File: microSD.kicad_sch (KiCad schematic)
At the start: 10 parts, among them IC1 4050D, IC2 LP298XS, X1 MICROSD

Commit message: added drawing sheet
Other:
- title: (none) -> microSD
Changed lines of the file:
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@@
 	(generator_version "8.0")
 	(paper "A4")
+	(title_block
+		(title "microSD")
+		(date "2024-03-06")
+	)
 	(junction
 		(at 119.38 109.22)

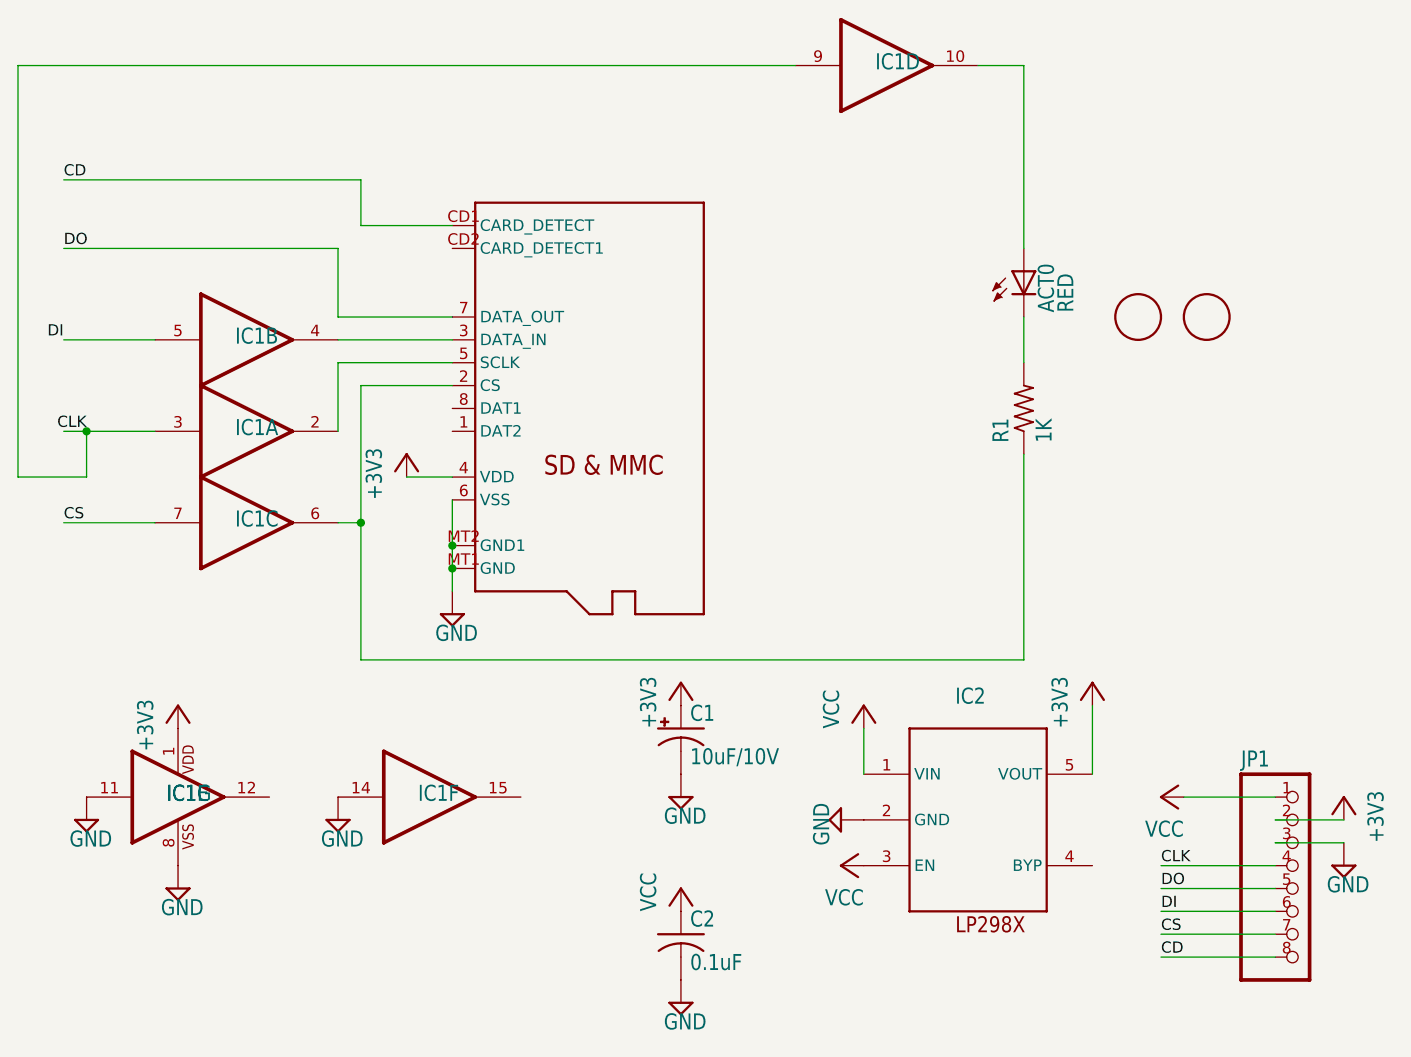
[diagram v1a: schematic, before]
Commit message: fully migrated to KiCad
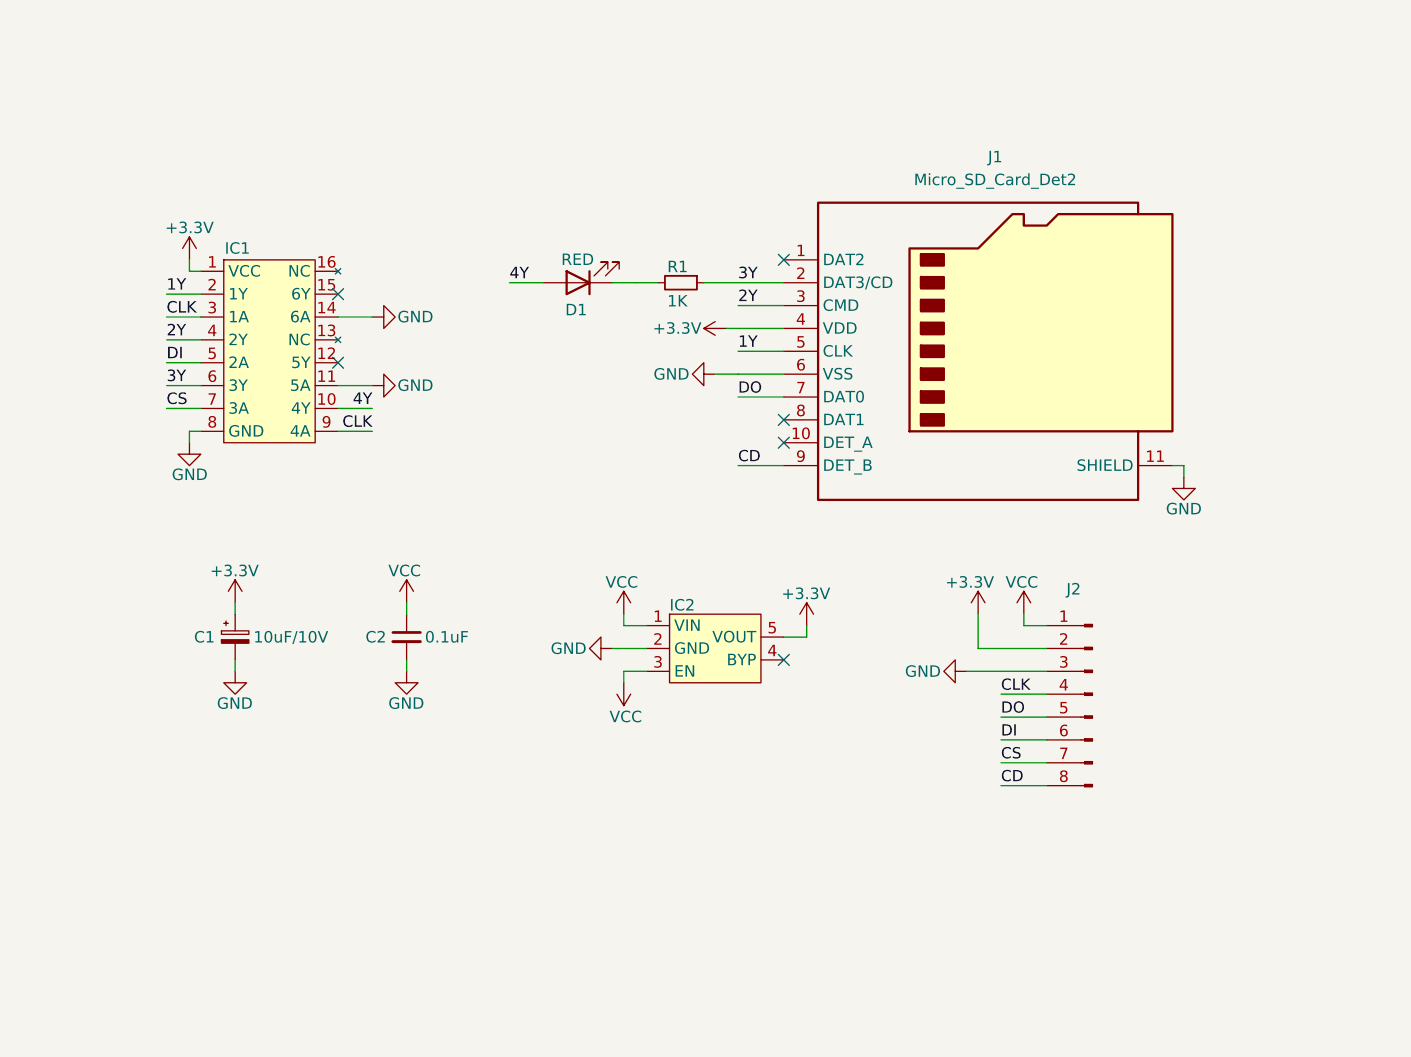
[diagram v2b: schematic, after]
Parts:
- removed ACT0: RED, microSD:CHIP-LED0805, symbol microSD-eagle-import:LEDCHIP-LED0805
- removed IC1: 4050D, microSD:SO16, symbol microSD-eagle-import:4050D
- removed R1: 1K, microSD:R0805, symbol microSD-eagle-import:R-US_R0805
- removed U$1, U$2: FIDUCIAL, microSD:FIDUCIAL_1MM, symbol microSD-eagle-import:FIDUCIAL
- removed X1: MICROSD, microSD:MICROSD, symbol microSD-eagle-import:MICROSD
- added D1: RED, LED_SMD:LED_0805_2012Metric, symbol Device:LED
- added IC1: ~, Package_SO:SOIC-16_3.9x9.9mm_P1.27mm, symbol external_library:74HC4050D
- added J1: Micro_SD_Card_Det2, external_footprints:GCT_MEM2061-01-188-00-A_REVA, symbol Connector:Micro_SD_Card_Det2
- added R1: 1K, Resistor_SMD:R_0805_2012Metric, symbol Device:R_Small
- C1: footprint microSD:A_3216-18R -> Capacitor_Tantalum_SMD:CP_EIA-3216-18_Kemet-A; symbol microSD-eagle-import:CPOL-USA/3216-18R -> Device:C_Polarized_Small
- C2: footprint microSD:C0805K -> Capacitor_SMD:C_0805_2012Metric; symbol microSD-eagle-import:C-USC0805K -> Device:C_Small
- IC2: footprint microSD:SOT23-5L -> Package_TO_SOT_SMD:SOT-23-5; symbol microSD-eagle-import:LP298XS -> external_library:LP2985A
- J2: renamed from JP1; footprint microSD:1X08-BIG -> Connector_PinHeader_2.54mm:PinHeader_1x08_P2.54mm_Vertical; symbol microSD-eagle-import:PINHD-1X8BIG -> Connector:Conn_01x08_Pin
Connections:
- net CD: now also J1.9 (DET_B)
- net CLK: now also IC1.3 (1A), IC1.9 (4A)
- net CS: now also IC1.7 (3A)
- net DI: now also IC1.5 (2A)
- net DO: now also J1.7 (DAT0)
- net GND: now also C1.2, IC1.11 (5A), IC1.14 (6A), IC1.8 (GND), J1.11 (SHIELD), J1.6 (VSS); no longer C1.-
- net +3V3 renamed +3.3V
- net +3.3V: now also C1.1, IC1.1 (VCC), J1.4 (VDD); no longer C1.+
- new net: D1.1 (K), R1.2
- new net 1Y: IC1.2 (1Y), J1.5 (CLK)
- new net 2Y: IC1.4 (2Y), J1.3 (CMD)
- new net 3Y: IC1.6 (3Y), J1.2 (DAT3/CD), R1.1
- new net 4Y: D1.2 (A), IC1.10 (4Y)
- no-connect marks 0 -> 6

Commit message: added info to generate BOM file
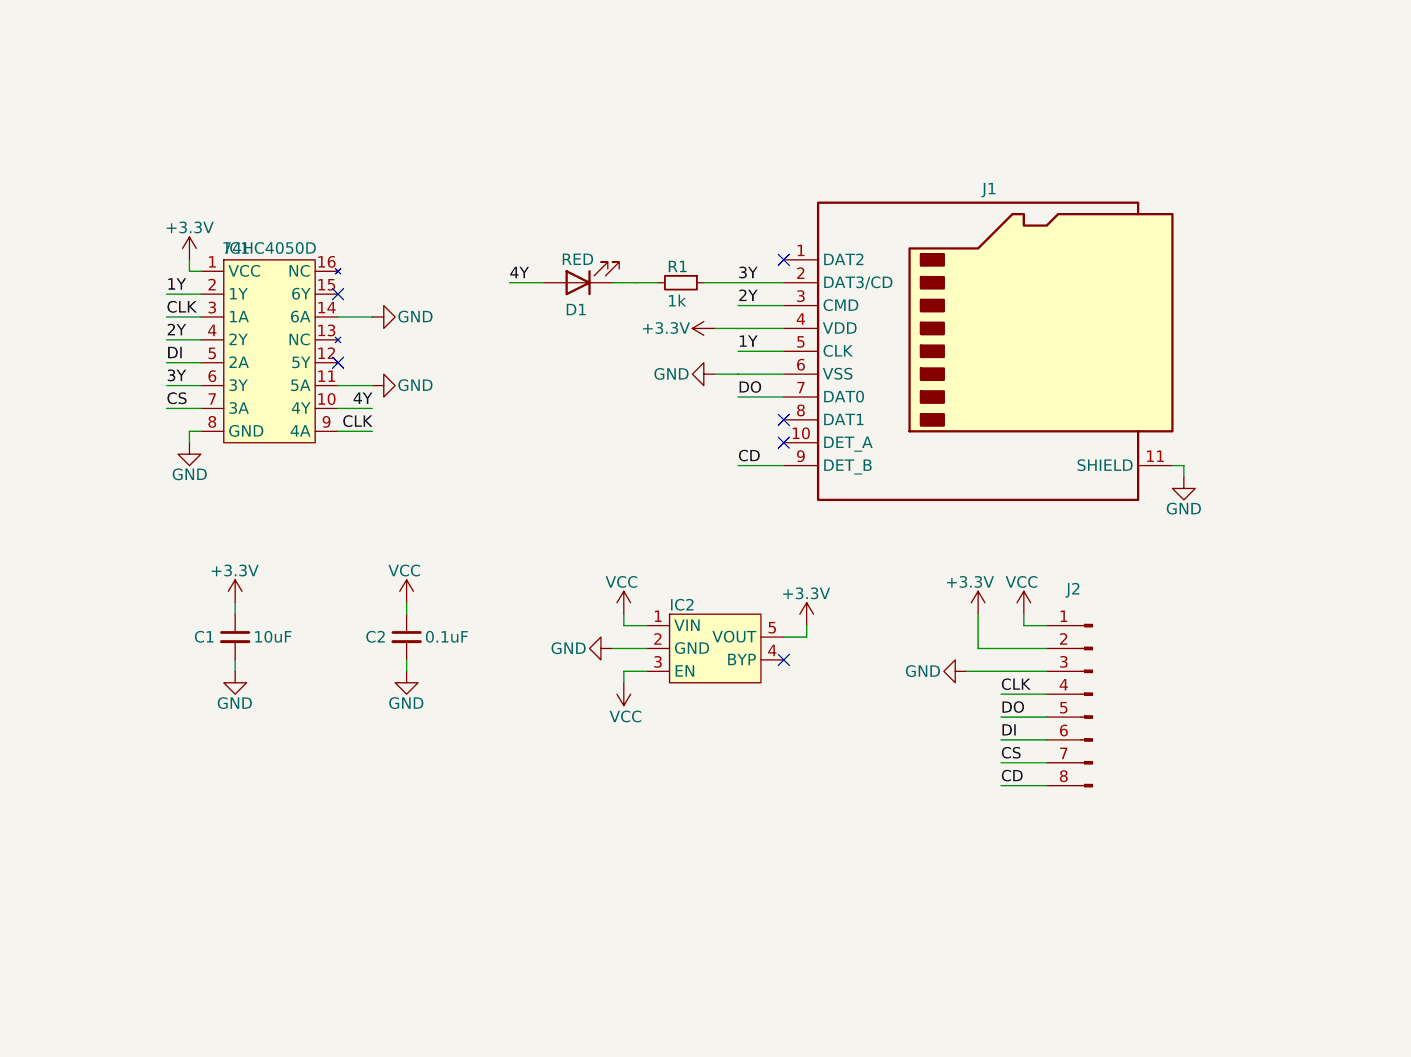
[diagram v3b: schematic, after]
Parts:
- C1: value 10uF/10V -> 10uF; footprint Capacitor_Tantalum_SMD:CP_EIA-3216-18_Kemet-A -> Capacitor_SMD:C_0805_2012Metric; symbol Device:C_Polarized_Small -> Device:C_Small; Component package type (none) -> 0805; MPN (none) -> /; Manufacturer (none) -> /; SPN (none) -> GPC0805106; Supplier (none) -> Eurocircuits
- C2: Component package type (none) -> 0805; MPN (none) -> /; Manufacturer (none) -> /; SPN (none) -> GPC0805104-100; Supplier (none) -> Eurocircuits
- D1: Component package type (none) -> 0805; MPN (none) -> 150080SS75000; Manufacturer (none) -> Würth Elektronik; SPN (none) -> 732-4985-1-ND; Supplier (none) -> DigiKey
- IC1: value ~ -> 74HC4050D; Component package type (none) -> 16-SOIC; MPN (none) -> 74HC4050D; Manufacturer (none) -> Toshiba Semiconductor and Storage; SPN (none) -> 74HC4050DCT-ND; Supplier (none) -> DigiKey
- IC2: value LP298XS -> LP2985A; Component package type (none) -> SOT-23-5; MPN (none) -> LP2985A-33DBVR; Manufacturer (none) -> Texas Instruments; SPN (none) -> 296-18479-1-ND; Supplier (none) -> DigiKey
- J1: value Micro_SD_Card_Det2 -> ~; Component package type (none) -> /; MPN (none) -> MEM2061-01-188-00-A; Manufacturer (none) -> GCT; SPN (none) -> 2073-MEM2061-01-188-00-ACT-ND; Supplier (none) -> DigiKey
- J2: value PINHD-1X8BIG -> ~; Component package type (none) -> /; MPN (none) -> TSW-108-23-G-S; Manufacturer (none) -> Samtec Inc.; SPN (none) -> 612-TSW-108-23-G-S-ND; Supplier (none) -> DigiKey
- R1: value 1K -> 1k; Component package type (none) -> /; MPN (none) -> /; Manufacturer (none) -> /; SPN (none) -> GPR08051K; Supplier (none) -> Eurocircuits

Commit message: minor fixes schematic and PCB
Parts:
- J1: value ~ -> microSD
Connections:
- no-connect marks 6 -> 8

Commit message: silkscreen + BOM update
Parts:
- R1: Component package type / -> R_0805
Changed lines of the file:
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@@
 			)
 		)
-		(property "Component package type" "/"
+		(property "Component package type" "R_0805"
 			(at 144.78 77.47 90)
 			(effects

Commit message: BOM presets update
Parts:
- C1, C2, D1: Component package type 0805 -> (none)
- IC1: Component package type 16-SOIC -> (none)
- IC2: Component package type SOT-23-5 -> (none)
- J1, J2: Component package type / -> (none)
- R1: Component package type R_0805 -> (none)
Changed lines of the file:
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@@
-			)
-		)
-		(property "Component package type" "/"
-			(at 190.5 123.19 0)
-			(effects
-				(font
-					(size 1.27 1.27)
-				)
-				(hide yes)
 			)
 		)
@@
 			)
 		)
-		(property "Component package type" "0805"
-			(at 133.35 77.47 0)
-			(effects
-				(font
-					(size 1.27 1.27)
-				)
-				(hide yes)
-			)
-		)
 		(pin "1"
 		)
@@
 		)
 		(property "SPN" "GPC0805106"
-			(at 95.25 116.84 0)
-			(effects
-				(font
-					(size 1.27 1.27)
-				)
-				(hide yes)
-			)
-		)
-		(property "Component package type" "0805"
 			(at 95.25 116.84 0)
 			(effects
@@
 			)
 		)
-		(property "Component package type" "0805"
-			(at 114.3 116.84 0)
-			(effects
-				(font
-					(size 1.27 1.27)
-				)
-				(hide yes)
-			)
-		)
 		(pin "1"
 		)
@@
 			)
 		)
-		(property "Component package type" "/"
-			(at 179.07 85.09 0)
-			(effects
-				(font
-					(size 1.27 1.27)
-				)
-				(hide yes)
-			)
-		)
 		(pin "6"
 		)
@@
 			)
 		)
-		(property "Component package type" "SOT-23-5"
-			(at 143.51 121.92 0)
-			(effects
-				(font
-					(size 1.27 1.27)
-				)
-				(hide yes)
-			)
-		)
 		(pin "1"
 		)
@@
 			)
 		)
-		(property "Component package type" "16-SOIC"
-			(at 93.98 95.25 0)
-			(effects
-				(font
-					(size 1.27 1.27)
-				)
-				(hide yes)
-			)
-		)
 		(pin "1"
 		)
@@
 			(at 144.78 77.47 90)
 			(effects
-				(font
-					(size 1.27 1.27)
-				)
-				(hide yes)
-			)
-		)
-		(property "Component package type" "R_0805"
-			(at 144.78 77.47 90)
-			(effects
